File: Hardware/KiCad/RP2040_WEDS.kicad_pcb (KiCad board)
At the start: 2 copper layers, 55 x 66 mm, 69 parts, among them J1 Barrel_Jack_Switch_Pin3Ring, J3 LiPo Batt, J5 Conn_02x05_Odd_Even, J6 SMA-J-P-H-RA-TH1, Q1 Q_PMOS_DGS, Q2 Q_PMOS_DGS, U1 RP2040, U2 MCP73831-2-OT, U3 W25Q128JVS, U4 BME280, U5 AP2112K-3.3, U6 LoRa-E5, U7 TPL5110, Y1 Crystal_GND24

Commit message: Signed-off-by: VizualCommander <99371988+VizualCommander@users.noreply.github.com>
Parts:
- added C24: 1uF, Capacitor_SMD:C_0603_1608Metric, F.Cu at (170.0, 72.3)
- added JP2: SolderJumper_2_Open, Jumper:SolderJumper-2_P1.3mm_Open_RoundedPad1.0x1.5mm, F.Cu at (176.0, 93.0)
- added R15: 27.4, Resistor_SMD:R_0603_1608Metric, F.Cu at (180.4, 68.1)
- added R16: 27.4, Resistor_SMD:R_0603_1608Metric, F.Cu at (178.6, 68.1)
- added USB: USB Header, Connector_PinHeader_1.27mm:PinHeader_1x04_P1.27mm_Vertical, F.Cu at (202.8, 54.5)
- C13: value 10uF -> 1uF
- J2: renamed from ANALOG; value Conn_01x03_Male -> Analog Soil Header
- J4: renamed from I2C; value Conn_01x04_Male -> I2C Soil Header
- NANO: renamed from NANO TMR
- SOIL: renamed from SOIL SIG
- moved TX 6.50 mm to (163.2, 67.3)
- moved R4 5.02 mm to (187.9, 61.6), turned to 90 degrees
- moved C16 4.85 mm to (163.0, 85.2), turned to 0 degrees
- moved R12 4.21 mm to (169.2, 57.6), turned to 0 degrees
- moved R9 4.00 mm to (161.1, 78.6)
- moved U4 4.00 mm to (161.1, 82.0)
- moved R8 4.00 mm to (161.1, 76.5)
- moved VDC 3.57 mm to (167.1, 92.3)
- moved C14 3.28 mm to (159.0, 85.2), turned to 180 degrees
- moved C11 3.19 mm to (174.9, 68.1)
- moved C4 3.16 mm to (176.7, 68.1)
- moved R5 2.50 mm to (192.5, 53.9)
- moved C3 2.20 mm to (183.9, 72.7), turned to 0 degrees
- moved C1 2.07 mm to (184.2, 69.8)
- moved VDD 2.00 mm to (156.1, 72.7)
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- renumbered LORA_RX to RX, LORA to SW3, LORA_TX to TX
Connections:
- J5 pad 6: (no net) -> unconnected-(J5-Pad6)
- J5 pad 8: (no net) -> unconnected-(J5-Pad8)
- U1 pad 13: (no net) -> unconnected-(U1-Pad13)
- U1 pad 14: (no net) -> unconnected-(U1-Pad14)
- U1 pad 15: (no net) -> unconnected-(U1-Pad15)
- U1 pad 16: (no net) -> unconnected-(U1-Pad16)
- U1 pad 17: (no net) -> unconnected-(U1-Pad17)
- U1 pad 18: (no net) -> unconnected-(U1-Pad18)
- U1 pad 2: (no net) -> unconnected-(U1-Pad2)
- U1 pad 27: (no net) -> unconnected-(U1-Pad27)
- U1 pad 28: (no net) -> unconnected-(U1-Pad28)
- U1 pad 3: (no net) -> unconnected-(U1-Pad3)
- U1 pad 30: (no net) -> unconnected-(U1-Pad30)
- U1 pad 31: (no net) -> unconnected-(U1-Pad31)
- U1 pad 32: (no net) -> unconnected-(U1-Pad32)
- U1 pad 34: (no net) -> unconnected-(U1-Pad34)
- U1 pad 35: (no net) -> unconnected-(U1-Pad35)
- U1 pad 39: (no net) -> unconnected-(U1-Pad39)
- U1 pad 4: (no net) -> unconnected-(U1-Pad4)
- U1 pad 40: (no net) -> unconnected-(U1-Pad40)
- U1 pad 41: (no net) -> unconnected-(U1-Pad41)
- U1 pad 46: (no net) -> /D-
- U1 pad 47: (no net) -> /D+
- U1 pad 48: (no net) -> VDD
- U1 pad 5: (no net) -> unconnected-(U1-Pad5)
- U1 pad 8: (no net) -> unconnected-(U1-Pad8)
- U1 pad 9: (no net) -> unconnected-(U1-Pad9)
- U2 pad 4: VDC -> Net-(U2-Pad4)
- U5 pad 4: (no net) -> unconnected-(U5-Pad4)
- U6 pad 11: (no net) -> unconnected-(U6-Pad11)
- U6 pad 12: (no net) -> unconnected-(U6-Pad12)
- U6 pad 13: (no net) -> unconnected-(U6-Pad13)
- U6 pad 14: (no net) -> unconnected-(U6-Pad14)
- U6 pad 18: (no net) -> unconnected-(U6-Pad18)
- U6 pad 19: (no net) -> unconnected-(U6-Pad19)
- U6 pad 20: (no net) -> unconnected-(U6-Pad20)
- U6 pad 21: (no net) -> unconnected-(U6-Pad21)
- U6 pad 23: (no net) -> unconnected-(U6-Pad23)
- U6 pad 25: (no net) -> unconnected-(U6-Pad25)
- U6 pad 26: (no net) -> unconnected-(U6-Pad26)
- U6 pad 27: (no net) -> unconnected-(U6-Pad27)
- U6 pad 28: (no net) -> unconnected-(U6-Pad28)
- U6 pad 3: (no net) -> unconnected-(U6-Pad3)
- U6 pad 4: (no net) -> unconnected-(U6-Pad4)
- U6 pad 5: (no net) -> unconnected-(U6-Pad5)
- U6 pad 6: (no net) -> unconnected-(U6-Pad6)
- U6 pad 7: (no net) -> unconnected-(U6-Pad7)
- U6 pad 8: (no net) -> unconnected-(U6-Pad8)
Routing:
- net VDC: track 46.0 -> 140.1 mm, vias 0 -> 1
- net USB_DP: track 0.00 -> 29.4 mm
- net USB_DN: track 0.00 -> 27.0 mm
- net GND: track 118.7 -> 143.8 mm, vias 40 -> 43
- net QSPI_SD1: track 19.5 -> 26.6 mm
- net QSPI_SD2: track 18.5 -> 25.5 mm
- net VDD: track 258.5 -> 252.2 mm, vias 14 -> 13
- net /D-: track 0.00 -> 5.47 mm
- net /D+: track 0.00 -> 5.45 mm
- net QSPI_CSN: track 24.3 -> 29.4 mm
- net +1V1: track 25.7 -> 30.7 mm
- net QSPI_SD0: track 15.0 -> 19.7 mm
- net QSPI_CLK: track 13.5 -> 18.2 mm
- net QSPI_SD3: track 12.0 -> 16.4 mm
- net Net-(R12-Pad1): track 7.19 -> 2.79 mm
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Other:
- net class Default removed

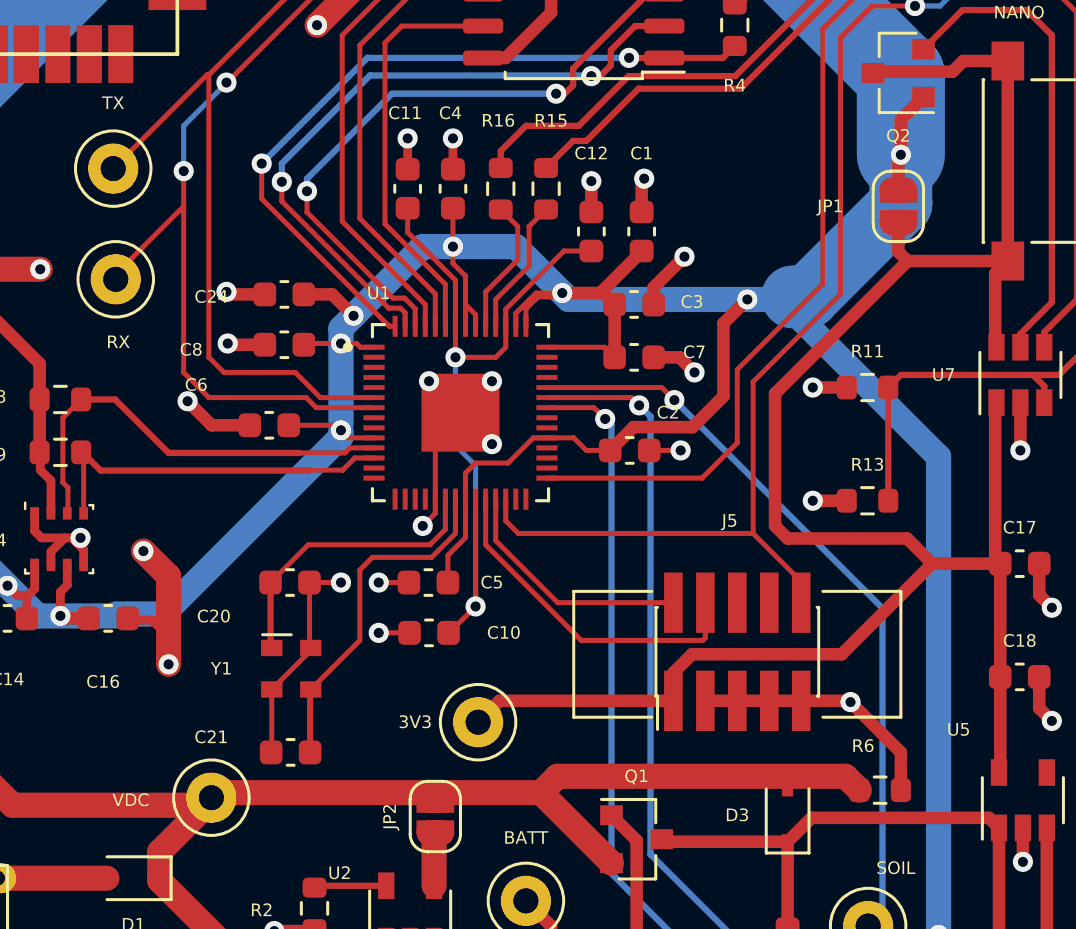
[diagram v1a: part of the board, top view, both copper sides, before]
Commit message: changed solder bridge position between 3V3 and VDD
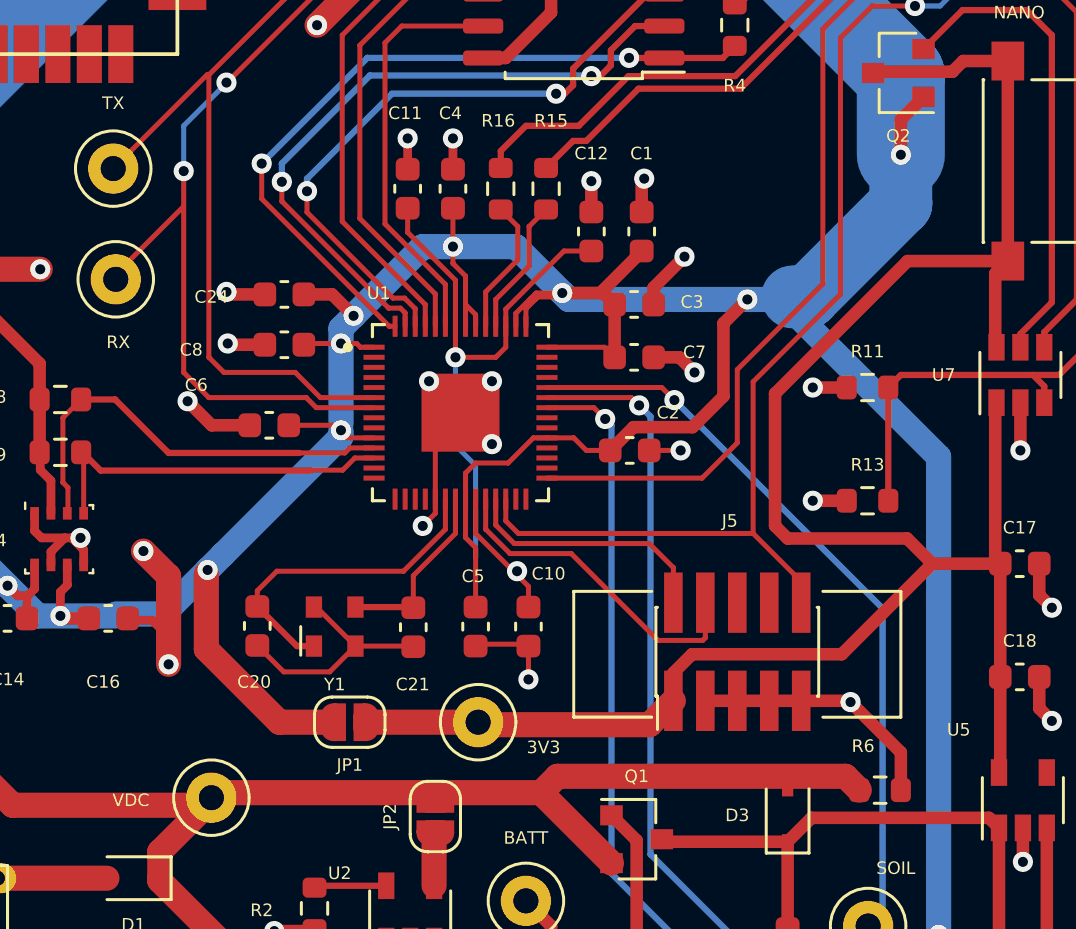
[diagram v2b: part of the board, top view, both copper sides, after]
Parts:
- moved JP1 29.9 mm to (172.6, 89.3), turned to 180 degrees
- moved C21 6.97 mm to (175.1, 85.5), turned to 90 degrees
- moved C10 3.96 mm to (179.7, 85.5), turned to -90 degrees
- moved C5 2.56 mm to (177.6, 85.5), turned to -90 degrees
- moved Y1 2.40 mm to (172.0, 85.5), turned to 0 degrees
- moved C20 2.16 mm to (168.9, 85.5), turned to -90 degrees
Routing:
- net VDD: track 252.2 -> 261.0 mm, vias 13 -> 14
- net XOUT: track 13.8 -> 7.32 mm
- net +3V3: track 81.2 -> 84.1 mm
- net +1V1: track 30.7 -> 28.2 mm
- net XIN: track 11.6 -> 13.2 mm
- net GND: track 143.8 -> 145.4 mm, vias 43 -> 41

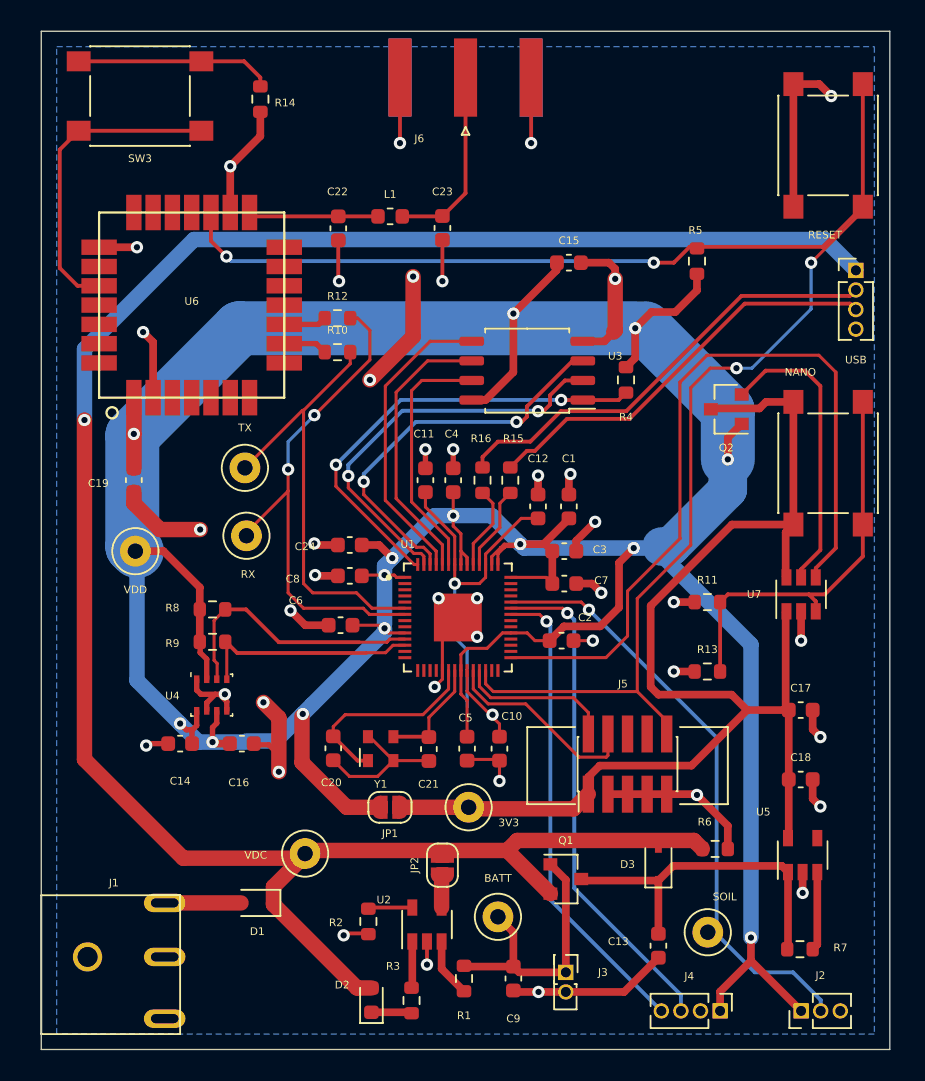
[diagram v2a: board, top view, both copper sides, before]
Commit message: Rearranged components around lipo charger
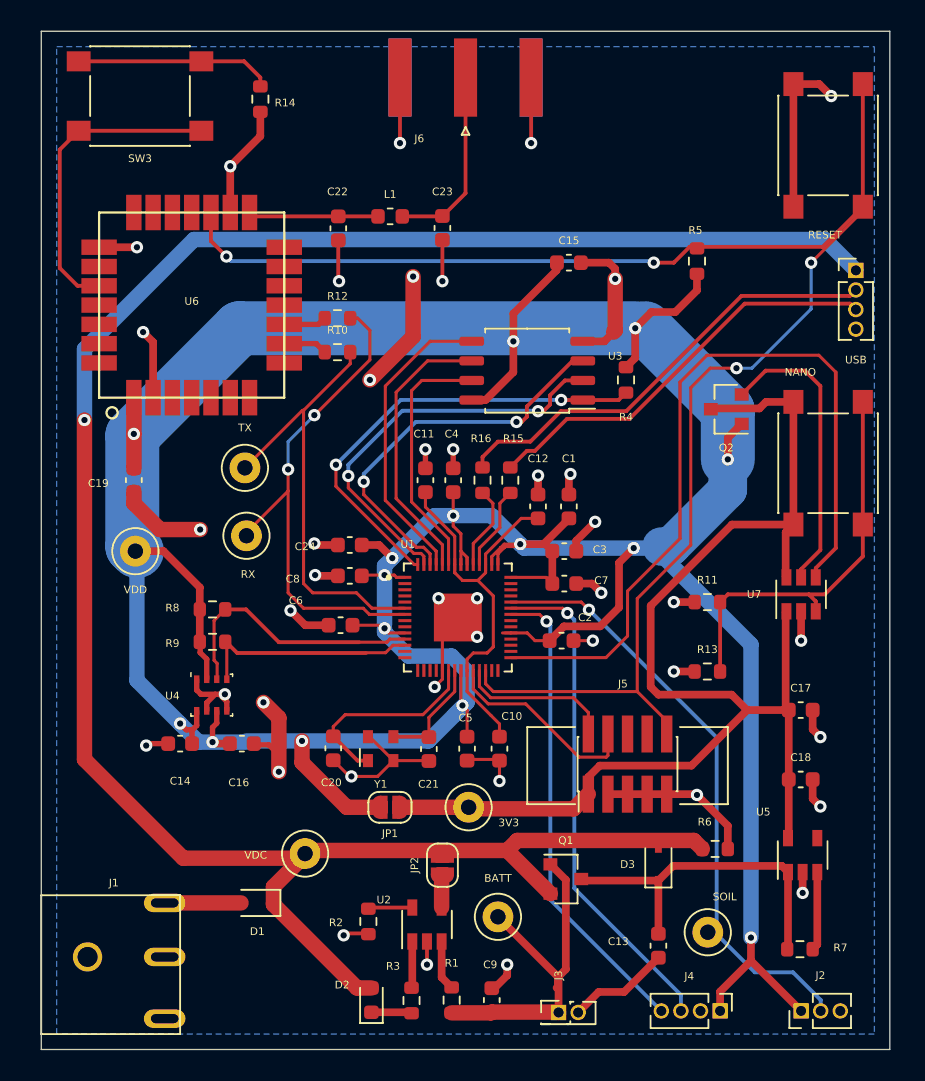
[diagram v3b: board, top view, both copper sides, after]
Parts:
- moved J3 2.64 mm to (183.5, 102.6), turned to 0 degrees
- moved C9 1.98 mm to (179.2, 101.8), turned to 90 degrees
- moved R1 1.61 mm to (176.6, 101.8), turned to 90 degrees
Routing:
- net VDD: track 261.0 -> 267.5 mm, vias 14 -> 15
- net +BATT: track 17.8 -> 23.5 mm
- net GND: track 145.4 -> 143.7 mm, vias 41 -> 42
- net +1V1: track 28.2 -> 26.6 mm, vias 2 -> 0
- net Net-(R1-Pad2): track 3.83 -> 3.24 mm

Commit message: changes
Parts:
- moved C1 14.4 mm to (170.0, 72.3), turned to 180 degrees
- moved C19 14.1 mm to (152.5, 54.4)
- moved R12 13.9 mm to (161.0, 68.8), turned to -90 degrees
- moved C24 13.2 mm to (183.2, 71.7), turned to 0 degrees
- moved R10 13.2 mm to (158.7, 67.8), turned to -90 degrees
- moved C22 7.40 mm to (172.1, 58.6), turned to 0 degrees
- moved L1 4.83 mm to (171.5, 55.7), turned to 90 degrees
- moved C23 3.86 mm to (172.2, 52.4), turned to 0 degrees
- moved TX 3.11 mm to (165.4, 69.5)
- moved RX 2.88 mm to (160.6, 72.7)
- moved U6 2.10 mm to (161.8, 57.2), turned to 0 degrees
- moved VDC 2.00 mm to (168.3, 93.9)
- moved C3 0.99 mm to (183.2, 73.4)
- moved C12 0.98 mm to (183.2, 69.7), turned to 0 degrees
- moved C7 0.76 mm to (183.2, 75.1)
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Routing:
- net LORA_RX: track 33.0 -> 18.7 mm, vias 2 -> 0
- net GND: track 143.7 -> 152.6 mm, vias 42 -> 39
- net LORA_TX: track 28.8 -> 21.3 mm
- net RESET: track 108.5 -> 102.6 mm
- net Net-(C23-Pad1): track 12.2 -> 17.9 mm
- net Net-(SW3-Pad1): track 20.4 -> 14.8 mm
- net VDD: track 267.5 -> 271.7 mm
- net Net-(R12-Pad1): track 2.79 -> 4.96 mm
- net Net-(R10-Pad1): track 2.85 -> 4.02 mm
- net Net-(C22-Pad1): track 8.43 -> 7.31 mm
- net QSPI_SD3: track 16.4 -> 15.5 mm
- net QSPI_CLK: track 18.2 -> 17.3 mm
- net +BATT: track 23.5 -> 22.7 mm
- net QSPI_SD0: track 19.7 -> 19.0 mm
- net +3V3: track 84.1 -> 84.7 mm

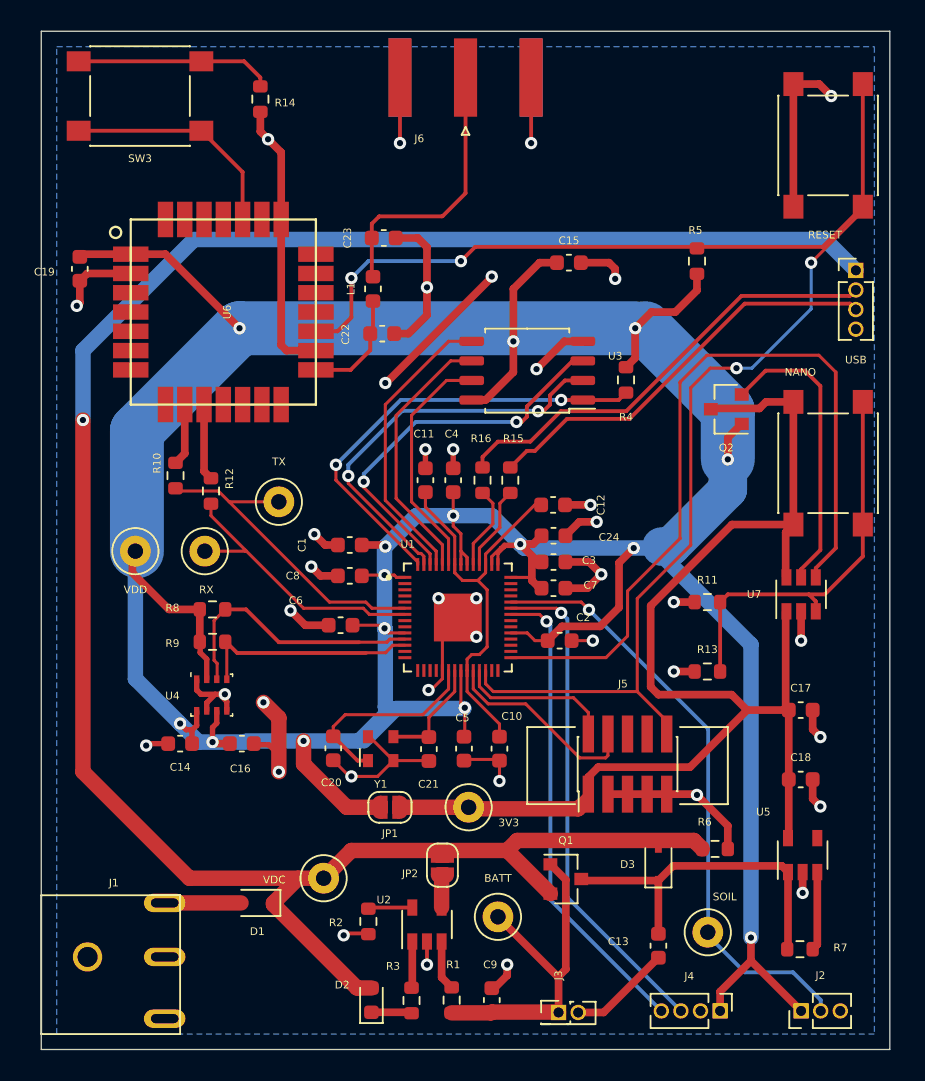
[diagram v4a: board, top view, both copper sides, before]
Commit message: Added power fills for 3V3, VDD and VDC
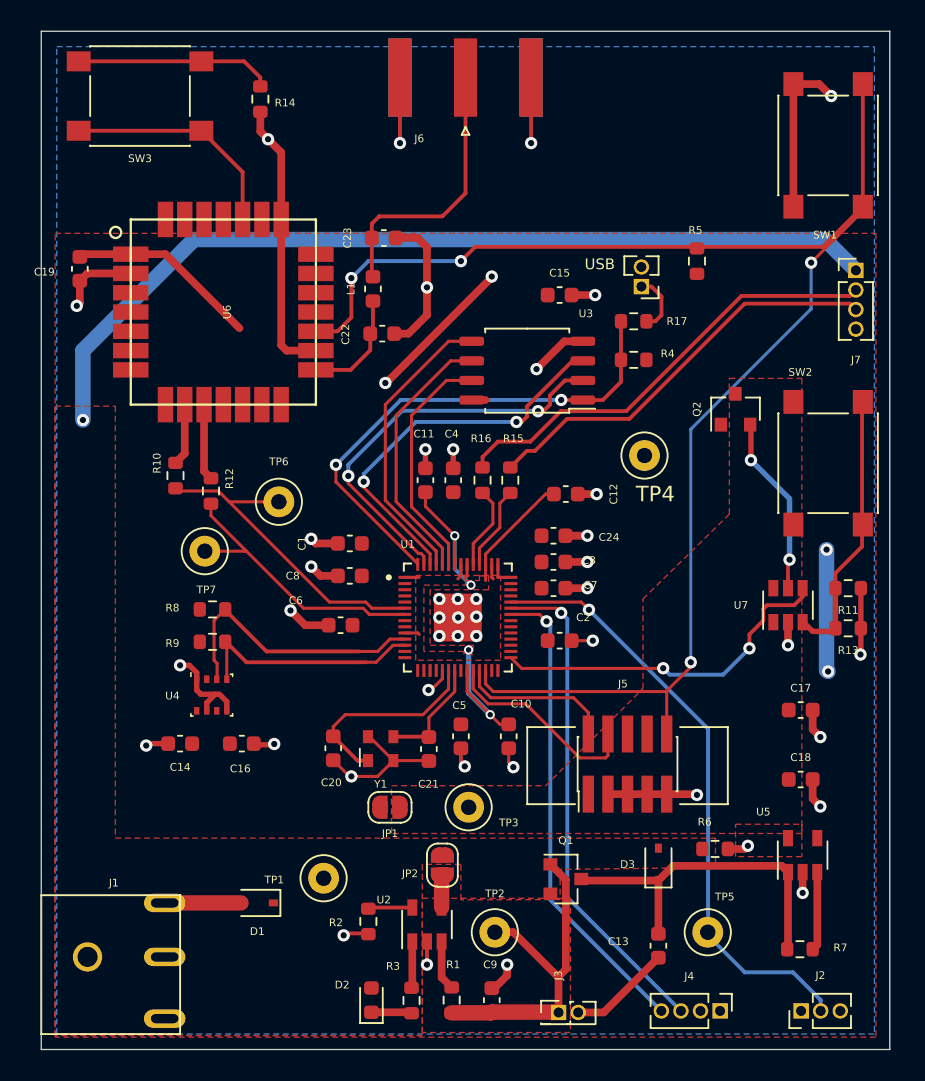
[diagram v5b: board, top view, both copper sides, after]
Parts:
- removed G***: LOGO, RP2040_WEDS:Flame_Logo
- removed VDD: TestPoint, TestPoint:TestPoint_Loop_D1.80mm_Drill1.0mm_Beaded
- added R17: 1k, Resistor_SMD:R_0603_1608Metric, F.Cu at (188.4, 57.8)
- added TP4: TestPoint, TestPoint:TestPoint_Loop_D1.80mm_Drill1.0mm_Beaded, F.Cu at (189.1, 66.5)
- added USB: Conn_01x02_Male, Connector_PinHeader_1.27mm:PinHeader_1x02_P1.27mm_Vertical, F.Cu at (188.9, 55.5)
- moved R13 9.54 mm to (202.3, 77.7), turned to 180 degrees
- moved R11 9.17 mm to (202.3, 75.1), turned to 180 degrees
- moved C15 2.18 mm to (183.6, 56.1)
- moved R4 1.39 mm to (188.4, 60.3), turned to 0 degrees
- moved U7 1.10 mm to (198.4, 76.2)
- moved C12 1.08 mm to (184.0, 69.0)
- moved TP2 1.02 mm to (179.4, 97.4)
- moved C10 1.00 mm to (180.3, 84.7)
- moved C5 0.82 mm to (177.2, 84.7)
- moved Q2 0.60 mm to (195.0, 63.5), turned to 90 degrees
- moved C1 0.10 mm to (170.0, 72.2)
- renumbered USB to J7, RESET to SW1, NANO to SW2, VDC to TP1, BATT to TP2, 3V3 to TP3, SOIL to TP5, TX to TP6, RX to TP7
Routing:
- net VDD: track 271.7 -> 27.9 mm, vias 15 -> 2
- net +3V3: track 84.7 -> 0.14 mm
- net VDC: track 140.4 -> 58.4 mm
- net DONE: track 51.1 -> 23.0 mm, vias 0 -> 2
- net GND: track 152.6 -> 137.1 mm, vias 39 -> 46
- net Net-(R11-Pad2): track 26.3 -> 18.0 mm
- net Net-(Q2-Pad2): track 19.1 -> 11.7 mm, vias 0 -> 2
- net QSPI_CSN: track 29.3 -> 33.3 mm
- net /~{USB_BOOT}: track 0.00 -> 3.91 mm
- net RESET: track 102.6 -> 100.5 mm
- net SDA: track 17.5 -> 18.0 mm
- net SCL: track 14.6 -> 15.1 mm
- net +1V1: vias 0 -> 4
- added copper zone on F.Cu, net +1V1
- added copper zone on F.Cu, net +3V3
- added copper zone on F.Cu, net +BATT
- added copper zone on F.Cu, net VDC
- added copper zone on F.Cu, net VDD
